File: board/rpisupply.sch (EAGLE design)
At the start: 33 parts, among them IC1 ATTINY45-20SU, Q1 IRF7416, Q2 BSS138, Q3 BSS138, Q4 IRF4905S, SW1 SCHURTER-LSH-1301.x, X1 MINI-USB, X2 AVR-ISP-6-EDGE

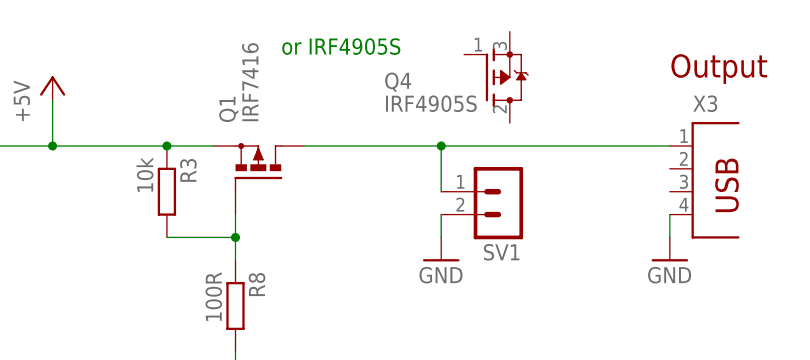
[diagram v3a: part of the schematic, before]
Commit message: change docs to mkdocs
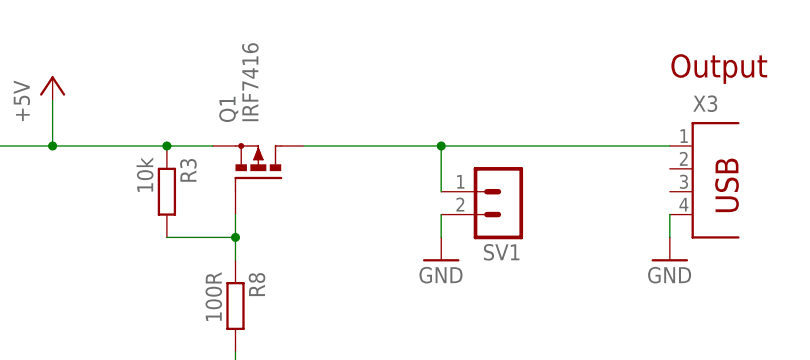
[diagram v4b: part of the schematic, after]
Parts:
- removed Q4: IRF4905S, transistor-fet:IRF4905S
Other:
- note removed: "or IRF4905S"
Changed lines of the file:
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@@
 <?xml version="1.0" encoding="utf-8"?>
 <!DOCTYPE eagle SYSTEM "eagle.dtd">
-<eagle version="7.4.0">
+<eagle version="7.5.0">
 <drawing>
 <settings>
@@
 <grid distance="0.1" unitdist="inch" unit="inch" style="lines" multiple="1" display="no" altdistance="0.01" altunitdist="inch" altunit="inch"/>
 <layers>
-<layer number="1" name="Top" color="4" fill="1" visible="yes" active="no"/>
-<layer number="2" name="Route2" color="1" fill="3" visible="yes" active="no"/>
-<layer number="3" name="Route3" color="4" fill="3" visible="yes" active="no"/>
-<layer number="4" name="Route4" color="1" fill="4" visible="yes" active="no"/>
-<layer number="5" name="Route5" color="4" fill="4" visible="yes" active="no"/>
-<layer number="6" name="Route6" color="1" fill="8" visible="yes" active="no"/>
-<layer number="7" name="Route7" color="4" fill="8" visible="yes" active="no"/>
-<layer number="8" name="Route8" color="1" fill="2" visible="yes" active="no"/>
-<layer number="9" name="Route9" color="4" fill="2" visible="yes" active="no"/>
-<layer number="10" name="Route10" color="1" fill="7" visible="yes" active="no"/>
-<layer number="11" name="Route11" color="4" fill="7" visible="yes" active="no"/>
-<layer number="12" name="Route12" color="1" fill="5" visible="yes" active="no"/>
-<layer number="13" name="Route13" color="4" fill="5" visible="yes" active="no"/>
-<layer number="14" name="Route14" color="1" fill="6" visible="yes" active="no"/>
-<layer number="15" name="Route15" color="4" fill="6" visible="yes" active="no"/>
-<layer number="16" name="Bottom" color="1" fill="1" visible="yes" active="no"/>
-<layer number="17" name="Pads" color="2" fill="1" visible="yes" active="no"/>
-<layer number="18" name="Vias" color="2" fill="1" visible="yes" active="no"/>
-<layer number="19" name="Unrouted" color="6" fill="1" visible="yes" active="no"/>
-<layer number="20" name="Dimension" color="15" fill="1" visible="yes" active="no"/>
-<layer number="21" name="tPlace" color="7" fill="1" visible="yes" active="no"/>
-<layer number="22" name="bPlace" color="7" fill="1" visible="yes" active="no"/>
-<layer number="23" name="tOrigins" color="15" fill="1" visible="yes" active="no"/>
-<layer number="24" name="bOrigins" color="15" fill="1" visible="yes" active="no"/>
-<layer number="25" name="tNames" color="7" fill="1" visible="yes" active="no"/>
-<layer number="26" name="bNames" color="7" fill="1" visible="yes" active="no"/>
-<layer number="27" name="tValues" color="7" fill="1" visible="yes" active="no"/>
-<layer number="28" name="bValues" color="7" fill="1" visible="yes" active="no"/>
+<layer number="1" name="Top" color="4" fill="1" visible="no" active="no"/>
+<layer number="2" name="Route2" color="1" fill="3" visible="no" active="no"/>
+<layer number="3" name="Route3" color="4" fill="3" visible="no" active="no"/>
+<layer number="4" name="Route4" color="1" fill="4" visible="no" active="no"/>
+<layer number="5" name="Route5" color="4" fill="4" visible="no" active="no"/>
+<layer number="6" name="Route6" color="1" fill="8" visible="no" active="no"/>
+<layer number="7" name="Route7" color="4" fill="8" visible="no" active="no"/>
+<layer number="8" name="Route8" color="1" fill="2" visible="no" active="no"/>
+<layer number="9" name="Route9" color="4" fill="2" visible="no" active="no"/>
+<layer number="10" name="Route10" color="1" fill="7" visible="no" active="no"/>
+<layer number="11" name="Route11" color="4" fill="7" visible="no" active="no"/>
+<layer number="12" name="Route12" color="1" fill="5" visible="no" active="no"/>
+<layer number="13" name="Route13" color="4" fill="5" visible="no" active="no"/>
+<layer number="14" name="Route14" color="1" fill="6" visible="no" active="no"/>
+<layer number="15" name="Route15" color="4" fill="6" visible="no" active="no"/>
+<layer number="16" name="Bottom" color="1" fill="1" visible="no" active="no"/>
+<layer number="17" name="Pads" color="2" fill="1" visible="no" active="no"/>
+<layer number="18" name="Vias" color="2" fill="1" visible="no" active="no"/>
+<layer number="19" name="Unrouted" color="6" fill="1" visible="no" active="no"/>
+<layer number="20" name="Dimension" color="15" fill="1" visible="no" active="no"/>
+<layer number="21" name="tPlace" color="7" fill="1" visible="no" active="no"/>
+<layer number="22" name="bPlace" color="7" fill="1" visible="no" active="no"/>
+<layer number="23" name="tOrigins" color="15" fill="1" visible="no" active="no"/>
+<layer number="24" name="bOrigins" color="15" fill="1" visible="no" active="no"/>
+<layer number="25" name="tNames" color="7" fill="1" visible="no" active="no"/>
+<layer number="26" name="bNames" color="7" fill="1" visible="no" active="no"/>
+<layer number="27" name="tValues" color="7" fill="1" visible="no" active="no"/>
+<layer number="28" name="bValues" color="7" fill="1" visible="no" active="no"/>
 <layer number="29" name="tStop" color="7" fill="3" visible="no" active="no"/>
 <layer number="30" name="bStop" color="7" fill="6" visible="no" active="no"/>
@@
 <layer number="35" name="tGlue" color="7" fill="4" visible="no" active="no"/>
 <layer number="36" name="bGlue" color="7" fill="5" visible="no" active="no"/>
-<layer number="37" name="tTest" color="7" fill="1" visible="yes" active="no"/>
-<layer number="38" name="bTest" color="7" fill="1" visible="yes" active="no"/>
+<layer number="37" name="tTest" color="7" fill="1" visible="no" active="no"/>
+<layer number="38" name="bTest" color="7" fill="1" visible="no" active="no"/>
 <layer number="39" name="tKeepout" color="4" fill="11" visible="no" active="no"/>
 <layer number="40" name="bKeepout" color="1" fill="11" visible="no" active="no"/>
@@
 <layer number="44" name="Drills" color="7" fill="1" visible="no" active="no"/>
 <layer number="45" name="Holes" color="7" fill="1" visible="no" active="no"/>
-<layer number="46" name="Milling" color="3" fill="1" visible="yes" active="no"/>
-<layer number="47" name="Measures" color="7" fill="1" visible="yes" active="no"/>
-<layer number="48" name="Document" color="7" fill="1" visible="yes" active="no"/>
-<layer number="49" name="Reference" color="7" fill="1" visible="yes" active="no"/>
-<layer number="50" name="dxf" color="7" fill="1" visible="yes" active="no"/>
-<layer number="51" name="tDocu" color="7" fill="1" visible="yes" active="no"/>
-<layer number="52" name="bDocu" color="7" fill="1" visible="yes" active="no"/>
+<layer number="46" name="Milling" color="3" fill="1" visible="no" active="no"/>
+<layer number="47" name="Measures" color="7" fill="1" visible="no" active="no"/>
+<layer number="48" name="Document" color="7" fill="1" visible="no" active="no"/>
+<layer number="49" name="Reference" color="7" fill="1" visible="no" active="no"/>
+<layer number="50" name="dxf" color="7" fill="1" visible="no" active="no"/>
+<layer number="51" name="tDocu" color="7" fill="1" visible="no" active="no"/>
+<layer number="52" name="bDocu" color="7" fill="1" visible="no" active="no"/>
 <layer number="91" name="Nets" color="2" fill="1" visible="yes" active="yes"/>
 <layer number="92" name="Busses" color="1" fill="1" visible="yes" active="yes"/>
@@
 <part name="P+8" library="supply1" deviceset="+5V" device=""/>
 <part name="Q3" library="transistor-fet" deviceset="BSS138" device="BSS138" value="BSS138"/>
-<part name="Q4" library="transistor-fet" deviceset="IRF4905S" device=""/>
 </parts>
 <sheets>
@@
 <text x="15.24" y="119.38" size="2.54" layer="94" font="vector">Input</text>
 <text x="127" y="119.38" size="2.54" layer="94" font="vector">Output</text>
-<text x="83.82" y="121.92" size="1.778" layer="91">or IRF4905S</text>
 <text x="142.24" y="43.18" size="1.778" layer="91">bidirectional levelshifter</text>
 <text x="200.66" y="53.34" size="1.778" layer="91">I2C PB0 PB2</text>
@@
 <instance part="P+8" gate="1" x="205.74" y="83.82"/>
 <instance part="Q3" gate="G$1" x="226.06" y="63.5" rot="MR270"/>
-<instance part="Q4" gate="G$1" x="106.68" y="119.38"/>
 </instances>
 <busses>
